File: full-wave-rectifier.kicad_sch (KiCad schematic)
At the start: 41 parts, among them J10 Control Right, J11 Main Right (mirrored), J2 Input Ch1, J3 Input Ch2, J4 Output Ch1, J5 Output Ch2, J6 Conn_01x01, J7 Conn_01x01, J8 Control Left, J9 Main Left (mirrored)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

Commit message: save changes
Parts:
- removed J7: Conn_01x01, Connector_PinHeader_2.54mm:PinHeader_1x01_P2.54mm_Vertical, symbol Connector_Generic:Conn_01x01
- removed unit 2 of POT1
- removed unit 2 of POT2
- removed unit 2 of POT3
- removed unit 2 of POT4
- J10, J8: footprint Connector_PinHeader_2.54mm:PinHeader_1x08_P2.54mm_Vertical -> Connector_PinSocket_2.54mm:PinSocket_1x08_P2.54mm_Vertical
- J11: value Main Right (mirrored) -> Main Right; footprint Connector_PinSocket_2.54mm:PinSocket_1x08_P2.54mm_Vertical -> Connector_PinHeader_2.54mm:PinHeader_1x08_P2.54mm_Vertical
- J6: value Conn_01x01 -> Ochd input; footprint Connector_PinHeader_2.54mm:PinHeader_1x01_P2.54mm_Vertical -> Connector_PinHeader_2.54mm:PinHeader_1x02_P2.54mm_Vertical; symbol Connector_Generic:Conn_01x01 -> Connector_Generic:Conn_01x02
- J9: value Main Left (mirrored) -> Main Left; footprint Connector_PinSocket_2.54mm:PinSocket_1x08_P2.54mm_Vertical -> Connector_PinHeader_2.54mm:PinHeader_1x08_P2.54mm_Vertical
- POT1, POT2, POT3, POT4: footprint 4ms_Potentiometer:Pot_9mm_DShaft -> Potentiometer_THT:Potentiometer_Alpha_RD901F-40-00D_Single_Vertical
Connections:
- net B_Ochd_2 is gone; now on net GND: J9.4 (Pin_4)
- net B_Offset_1: no longer J9.2 (Pin_2)
- net B_Offset_2: no longer J9.5 (Pin_5)
- net B_Output_1: no longer J11.1 (Pin_1)
- net B_Output_2: no longer J11.5 (Pin_5)
- net GND: now also J10.2 (Pin_2), J10.4 (Pin_4), J10.5 (Pin_5), J11.2 (Pin_2), J11.4 (Pin_4), J11.5 (Pin_5), J8.2 (Pin_2), J8.4 (Pin_4), J8.5 (Pin_5), J9.2 (Pin_2), J9.5 (Pin_5); no longer J10.7 (Pin_7), J11.7 (Pin_7), J8.7 (Pin_7), J9.7 (Pin_7)
- net T_Offset_1: no longer J8.2 (Pin_2)
- net T_Offset_2: no longer J8.5 (Pin_5)
- net T_Output_1: no longer J10.1 (Pin_1)
- net T_Output_2: no longer J10.5 (Pin_5)
- net +12V renamed OUTPUT_CH1
- net OUTPUT_CH1: now also J9.8 (Pin_8); no longer J11.8 (Pin_8)
- net -12V renamed OUTPUT_CH2
- net OUTPUT_CH2: now also J11.8 (Pin_8); no longer J9.8 (Pin_8)
- net B_Input_1 renamed INPUT_CH1
- net INPUT_CH1: now also J8.7 (Pin_7), J9.7 (Pin_7), U3.13 (-), U3.14; no longer J11.2 (Pin_2)
- net B_Input_2 renamed INPUT_CH2
- net INPUT_CH2: now also J10.7 (Pin_7), J11.7 (Pin_7), U3.6 (-), U3.7; no longer J11.4 (Pin_4)
- net B_Ochd_1 renamed OCHD_CH1
- net OCHD_CH1: now also J2.TN; no longer J9.1 (Pin_1)
- removed net T_Input_1: J10.2 (Pin_2), U3.13 (-), U3.14
- removed net T_Input_2: J10.4 (Pin_4), U3.6 (-), U3.7
- net T_Ochd_1 renamed OFFSET_CH1
- net OFFSET_CH1: now also J9.1 (Pin_1); no longer J2.TN
- net T_Ochd_2 renamed OCHD_CH2
- net OCHD_CH2: now also J6.2 (Pin_2); no longer J8.4 (Pin_4)
- new net OFFSET_CH2: J10.1 (Pin_1), J11.1 (Pin_1)
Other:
- moved on the sheet: J10, J11, J2, J3, J9, R3, R4, R5, R6, U3B, U3D

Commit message: save changes
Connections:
- net T_Offset_1 is gone; now on an unnamed net: POT2.1 (Left)
- net T_Offset_2 is gone; now on an unnamed net: POT4.1 (Left)
- net T_Output_1 is gone; now on an unnamed net: POT1.1 (Left)
- net T_Output_2 is gone; now on an unnamed net: POT3.1 (Left)
- net INPUT_CH1: now also R5.2, U3.12 (+); no longer R13.1, R14.2, U3.13 (-), U3.14
- net INPUT_CH2: now also R6.2, U3.5 (+); no longer R16.1, R17.2, U3.6 (-), U3.7
- net OUTPUT_CH1: now also R7.1, U3.1, U3.2 (-)
- net OUTPUT_CH2: now also R8.1, U3.8, U3.9 (-)
- net B_Offset_1: no longer names the net of U2.1, U2.2 (-)
- net B_Offset_2: no longer names the net of U2.6 (-), U2.7
- net B_Output_1: no longer names the net of R19.2, U4.1
- net B_Output_2: no longer names the net of R20.2, U4.14
- new net: R13.1, R14.2, U3.13 (-), U3.14
- new net: R16.1, R17.2, U3.6 (-), U3.7
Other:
- moved on the sheet: J2, J4, J5, R3, R5, R7, R8, U3A, U3B, U3C, U3D

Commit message: power
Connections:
- net +5V: now also U2.12 (+); no longer U2.5 (+)
- net GND: now also U2.10 (+), U2.5 (+); no longer U2.10 (+), U2.12 (+)
- new net: POT4.1 (Left), U2.13 (-), U2.14
- new net: U2.8, U2.9 (-)
- new net: U2.6 (-), U2.7
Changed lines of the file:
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@@
 		(at 163.83 137.16 0)
 		(mirror x)
-		(unit 2)
+		(unit 4)
 		(exclude_from_sim no)
 		(in_bom yes)
@@
 				(path "/662e1ec4-0bac-4d87-a66b-840368d21815"
 					(reference "U2")
-					(unit 2)
+					(unit 4)
 				)
 			)
@@
 		(at 157.48 184.15 0)
 		(mirror x)
-		(unit 4)
+		(unit 3)
 		(exclude_from_sim no)
 		(in_bom yes)
@@
 				(path "/662e1ec4-0bac-4d87-a66b-840368d21815"
 					(reference "U2")
-					(unit 4)
+					(unit 3)
 				)
 			)
@@
 		(at 157.48 162.56 0)
 		(mirror x)
-		(unit 3)
+		(unit 2)
 		(exclude_from_sim no)
 		(in_bom yes)
@@
 				(path "/662e1ec4-0bac-4d87-a66b-840368d21815"
 					(reference "U2")
-					(unit 3)
+					(unit 2)
 				)
 			)

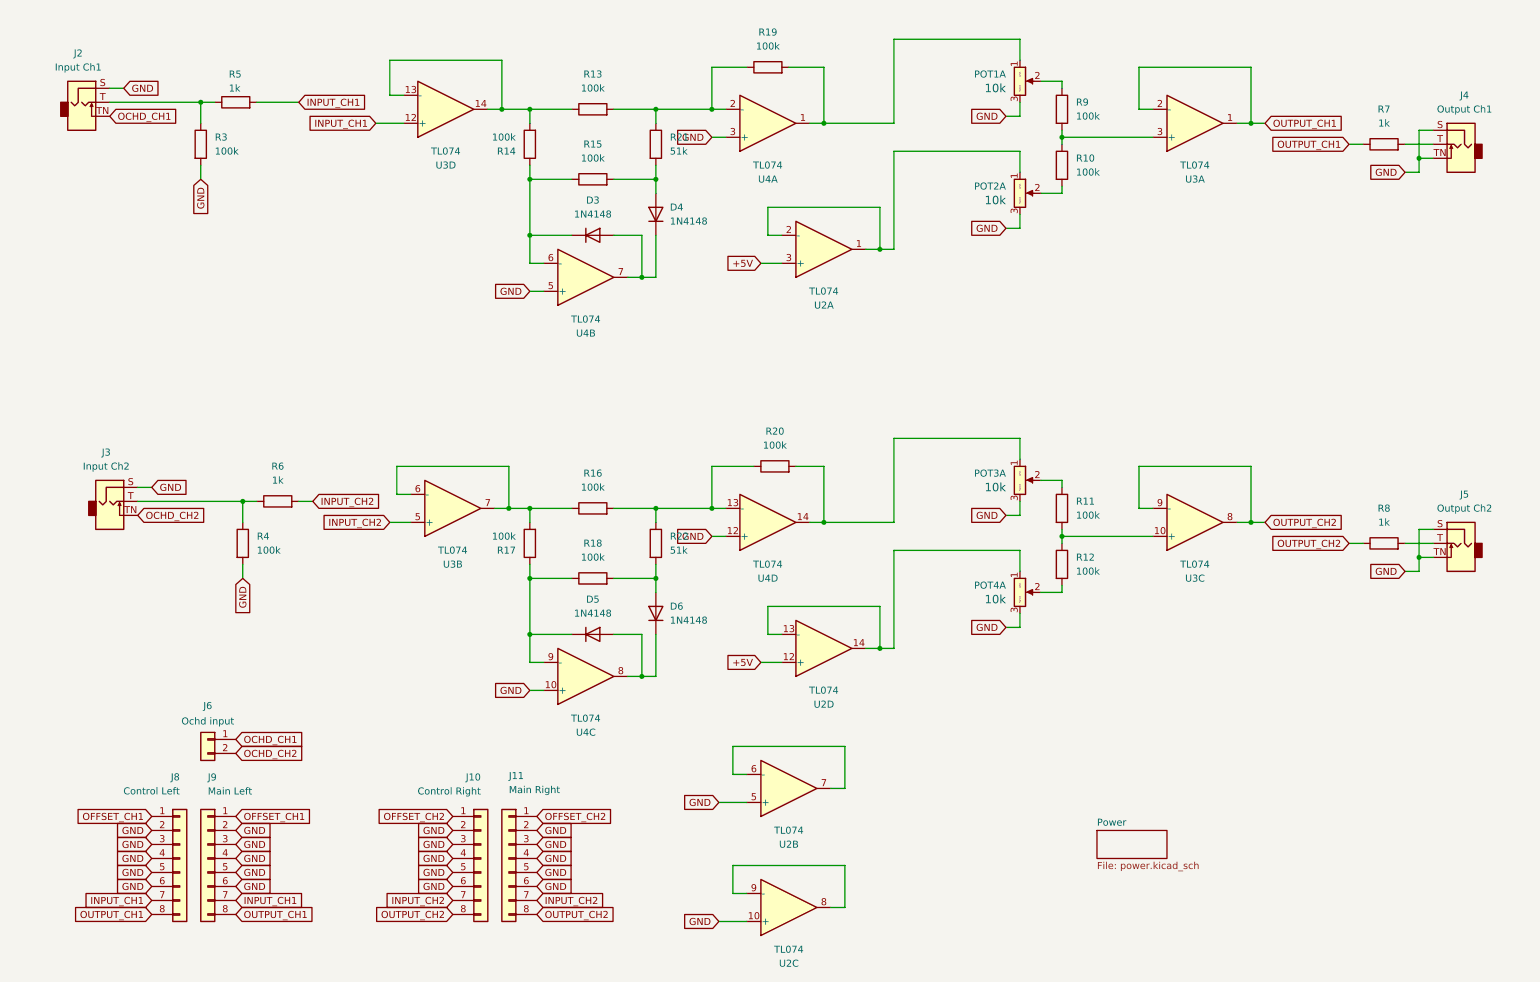
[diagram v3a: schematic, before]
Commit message: added rectifiers
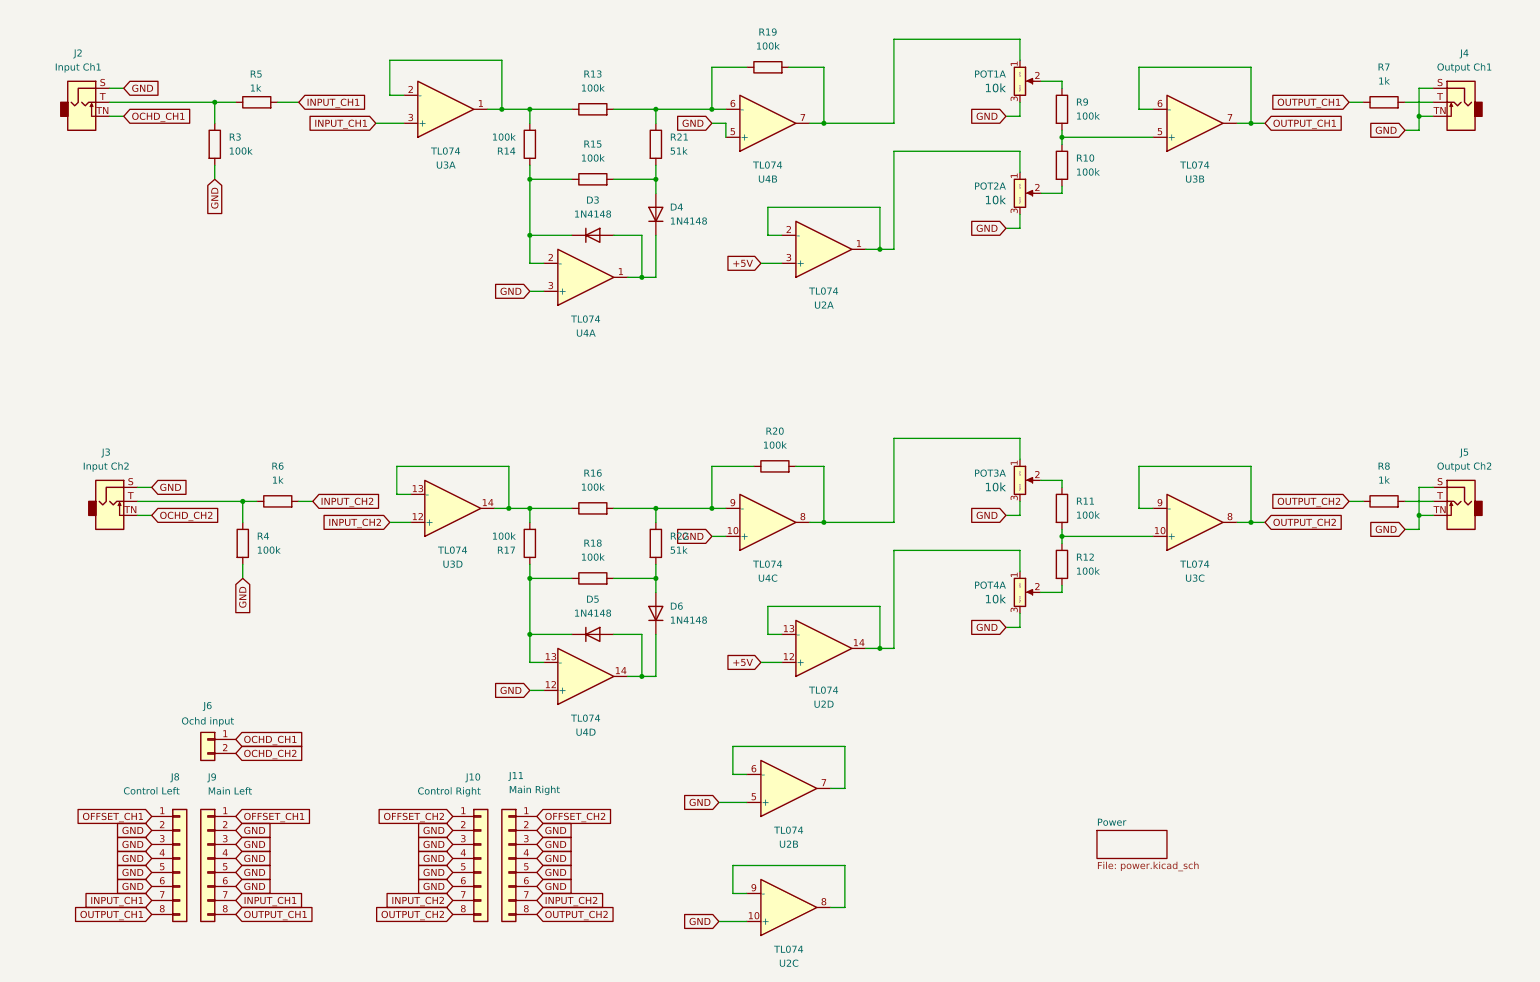
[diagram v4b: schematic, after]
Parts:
- D3, D4, D5, D6: footprint Diode_THT:D_DO-35_SOD27_P7.62mm_Horizontal -> Diode_SMD:D_SOD-123; symbol Diode:1N4148 -> Diode:1N4148W
- R13, R14, R15, R16, R17, R18, R19, R20: footprint Resistor_THT:R_Axial_DIN0207_L6.3mm_D2.5mm_P2.54mm_Vertical -> Resistor_SMD:R_1206_3216Metric_Pad1.30x1.75mm_HandSolder
- R21, R22: footprint Resistor_THT:R_Axial_DIN0207_L6.3mm_D2.5mm_P5.08mm_Vertical -> Resistor_SMD:R_1206_3216Metric_Pad1.30x1.75mm_HandSolder
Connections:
- net GND: now also U4.10 (+), U4.12 (+), U4.3 (+), U4.5 (+); no longer U4.10 (+), U4.12 (+), U4.3 (+), U4.5 (+)
- net INPUT_CH1: now also U3.3 (+); no longer U3.12 (+)
- net INPUT_CH2: now also U3.12 (+); no longer U3.5 (+)
- net OUTPUT_CH1: now also U3.6 (-), U3.7; no longer U3.1, U3.2 (-)
- net at R16.2, R20.1, R22.1: now also U4.9 (-); no longer U4.13 (-)
- net at R10.1, R9.2: now also U3.5 (+); no longer U3.3 (+)
- net at R13.1, R14.2: now also U3.1, U3.2 (-); no longer U3.13 (-), U3.14
- net at D5.2 (A), D6.1 (K): now also U4.14; no longer U4.8
- net at POT3.1 (Left), R20.2: now also U4.8; no longer U4.14
- net at D5.1 (K), R17.1, R18.1: now also U4.13 (-); no longer U4.9 (-)
- net at R16.1, R17.2: now also U3.13 (-), U3.14; no longer U3.6 (-), U3.7
- net at POT1.1 (Left), R19.2: now also U4.7; no longer U4.1
- net at D3.2 (A), D4.1 (K): now also U4.1; no longer U4.7
- net at R13.2, R19.1, R21.1: now also U4.6 (-); no longer U4.2 (-)
- net at D3.1 (K), R14.1, R15.1: now also U4.2 (-); no longer U4.6 (-)
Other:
- moved on the sheet: J4, J5, R3, R5, R7, R8

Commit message: save changes
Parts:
- R10, R11, R12, R3, R4, R9: footprint Resistor_THT:R_Axial_DIN0207_L6.3mm_D2.5mm_P2.54mm_Vertical -> Resistor_SMD:R_1206_3216Metric_Pad1.30x1.75mm_HandSolder
- R5, R6, R7, R8: footprint Resistor_THT:R_Axial_DIN0207_L6.3mm_D2.5mm_P5.08mm_Vertical -> Resistor_SMD:R_1206_3216Metric_Pad1.30x1.75mm_HandSolder
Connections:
- net GND: no longer J10.2 (Pin_2), J10.3 (Pin_3), J11.2 (Pin_2), J11.3 (Pin_3), J8.2 (Pin_2), J8.3 (Pin_3), J9.2 (Pin_2), J9.3 (Pin_3)
- net OFFSET_CH1: now also J8.2 (Pin_2), J9.2 (Pin_2), POT2.1 (Left), U2.1, U2.2 (-); no longer J8.1 (Pin_1), J9.1 (Pin_1)
- net OFFSET_CH2: now also J10.2 (Pin_2), J11.2 (Pin_2), POT4.1 (Left), U2.13 (-), U2.14; no longer J10.1 (Pin_1), J11.1 (Pin_1)
- net SUM_CH1: now reaches R10.1, R9.2, U3.5 (+)
- net SUM_CH1: now also J8.3 (Pin_3), J9.3 (Pin_3)
- net AMP_CH2: now reaches POT3.1 (Left), R20.2, U4.8
- net AMP_CH2: now also J10.1 (Pin_1), J11.1 (Pin_1)
- net AMP_CH1: now reaches POT1.1 (Left), R19.2, U4.7
- net AMP_CH1: now also J8.1 (Pin_1), J9.1 (Pin_1)
- net SUM_CH2: now reaches R11.2, R12.1, U3.10 (+)
- net SUM_CH2: now also J10.3 (Pin_3), J11.3 (Pin_3)
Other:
- moved on the sheet: J4, J5, POT1A, POT2A, POT3A, POT4A, R10, R11, R12, R19, R20, R7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

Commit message: save changes
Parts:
- added unit 2 of POT1
- added unit 2 of POT2
- added unit 2 of POT3
- added unit 2 of POT4
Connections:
- net AMP_CH2: now also J10.2 (Pin_2), J11.2 (Pin_2); no longer J10.1 (Pin_1), J11.1 (Pin_1)
- net GND: now also POT1.4 (Tab1), POT1.5 (Tab2), POT2.4 (Tab1), POT2.5 (Tab2), POT3.4 (Tab1), POT3.5 (Tab2), POT4.4 (Tab1), POT4.5 (Tab2)
- net OFFSET_CH1: now also J8.3 (Pin_3), J9.3 (Pin_3); no longer J8.2 (Pin_2), J9.2 (Pin_2)
- net OFFSET_CH2: now also J10.1 (Pin_1), J11.1 (Pin_1); no longer J10.2 (Pin_2), J11.2 (Pin_2)
- net SUM_CH1: now also J8.2 (Pin_2), J9.2 (Pin_2); no longer J8.3 (Pin_3), J9.3 (Pin_3)
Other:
- moved on the sheet: D3, D4, D5, D6, J2, J3, J4, J5, POT1A, POT2A, POT3A, POT4A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

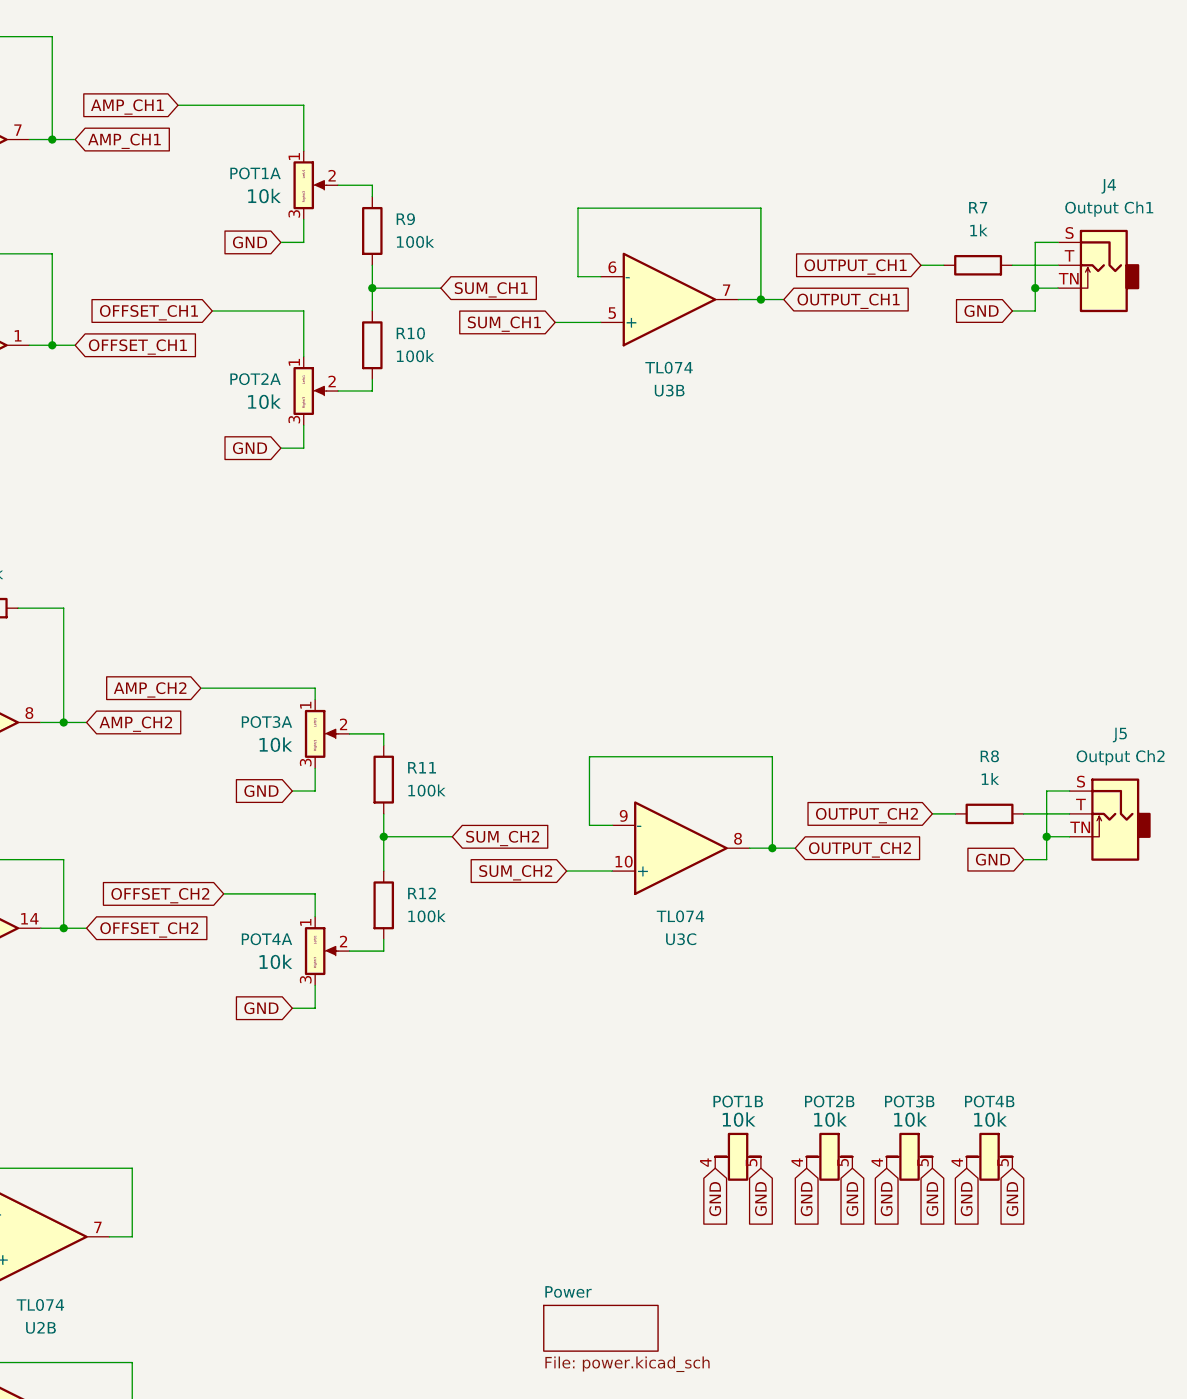
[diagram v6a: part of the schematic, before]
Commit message: updated footprints
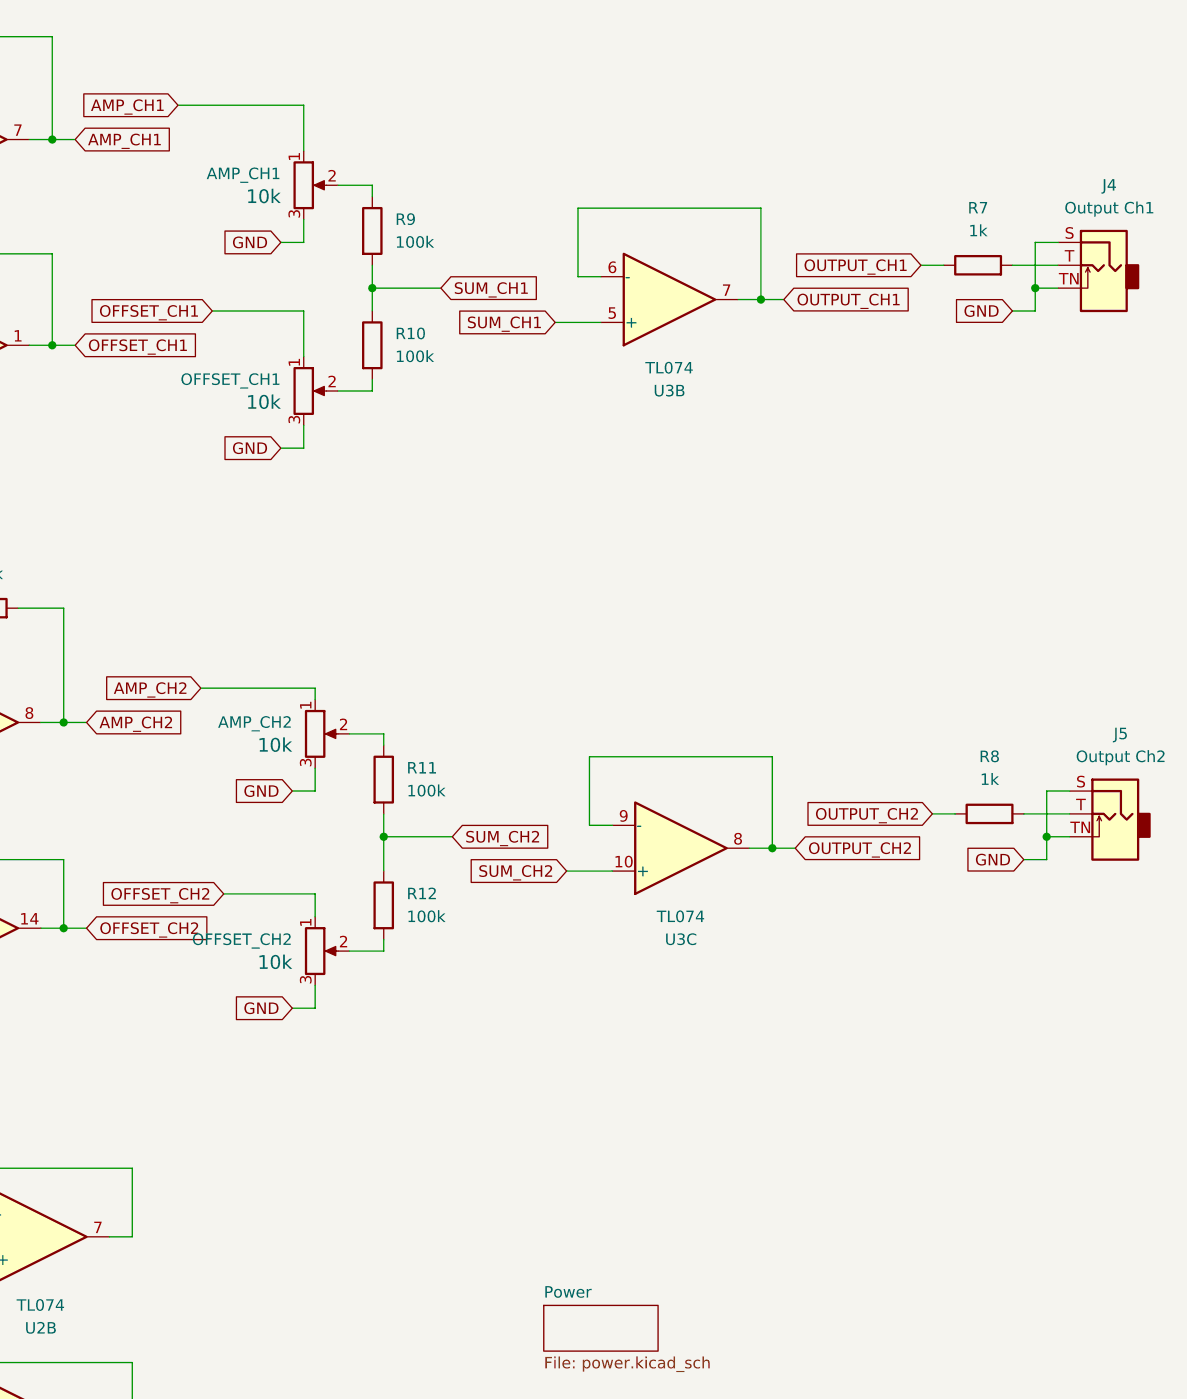
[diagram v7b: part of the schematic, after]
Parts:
- removed unit 2 of POT1
- removed unit 2 of POT2
- removed unit 2 of POT3
- removed unit 2 of POT4
- AMP_CH1: renamed from POT1; value 9mm_NoDet_10k_DShaft -> 10k; footprint Potentiometer_THT:Potentiometer_Alpha_RD901F-40-00D_Single_Vertical -> Eurorack:Pot_Alpha_9mm; symbol 4ms_Potentiometer:9mm_NoDet_10k_DShaft -> Device:R_Potentiometer
- AMP_CH2: renamed from POT3; value 9mm_NoDet_10k_DShaft -> 10k; footprint Potentiometer_THT:Potentiometer_Alpha_RD901F-40-00D_Single_Vertical -> Eurorack:Pot_Alpha_9mm; symbol 4ms_Potentiometer:9mm_NoDet_10k_DShaft -> Device:R_Potentiometer
- J2, J3, J4, J5: footprint AudioJacks:Jack_3.5mm_QingPu_WQP-PJ398SM_Vertical -> Eurorack:Jack_3.5mm_WQP518MA
- OFFSET_CH1: renamed from POT2; value 9mm_NoDet_10k_DShaft -> 10k; footprint Potentiometer_THT:Potentiometer_Alpha_RD901F-40-00D_Single_Vertical -> Eurorack:Pot_Alpha_9mm; symbol 4ms_Potentiometer:9mm_NoDet_10k_DShaft -> Device:R_Potentiometer
- OFFSET_CH2: renamed from POT4; value 9mm_NoDet_10k_DShaft -> 10k; footprint Potentiometer_THT:Potentiometer_Alpha_RD901F-40-00D_Single_Vertical -> Eurorack:Pot_Alpha_9mm; symbol 4ms_Potentiometer:9mm_NoDet_10k_DShaft -> Device:R_Potentiometer
